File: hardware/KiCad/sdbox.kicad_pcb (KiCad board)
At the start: 2 copper layers, 55 x 59 mm, 22 parts, among them J1 DB25_Male_MountingHoles, J2 Barrel_Jack, J5 Conn_01x01, J6 Conn_01x01, Q1 BC847BW, Q2 BC847BW, U1 Arduino_Nano_V3, U2 Micro_SD_Card_Module, U3 PVG612S

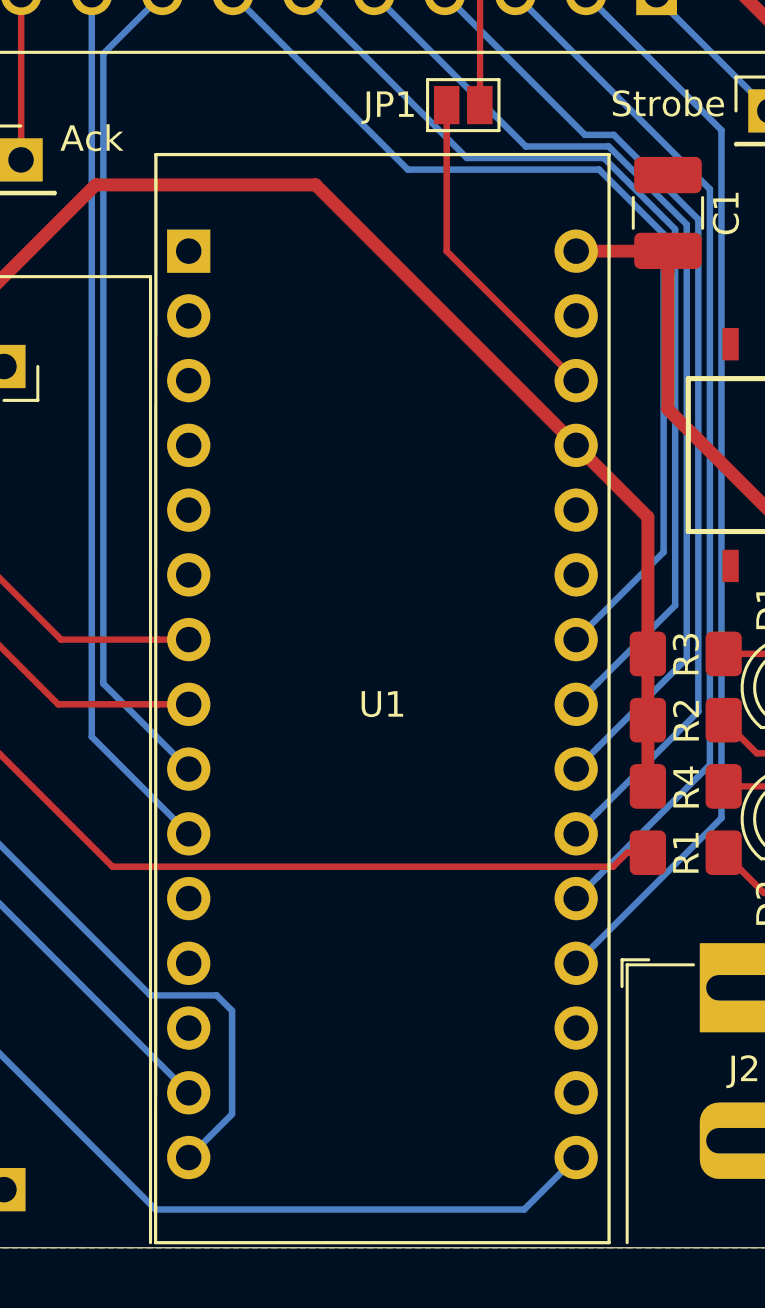
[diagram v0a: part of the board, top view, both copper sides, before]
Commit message: fixed symbol and footprint libs now included as project libs
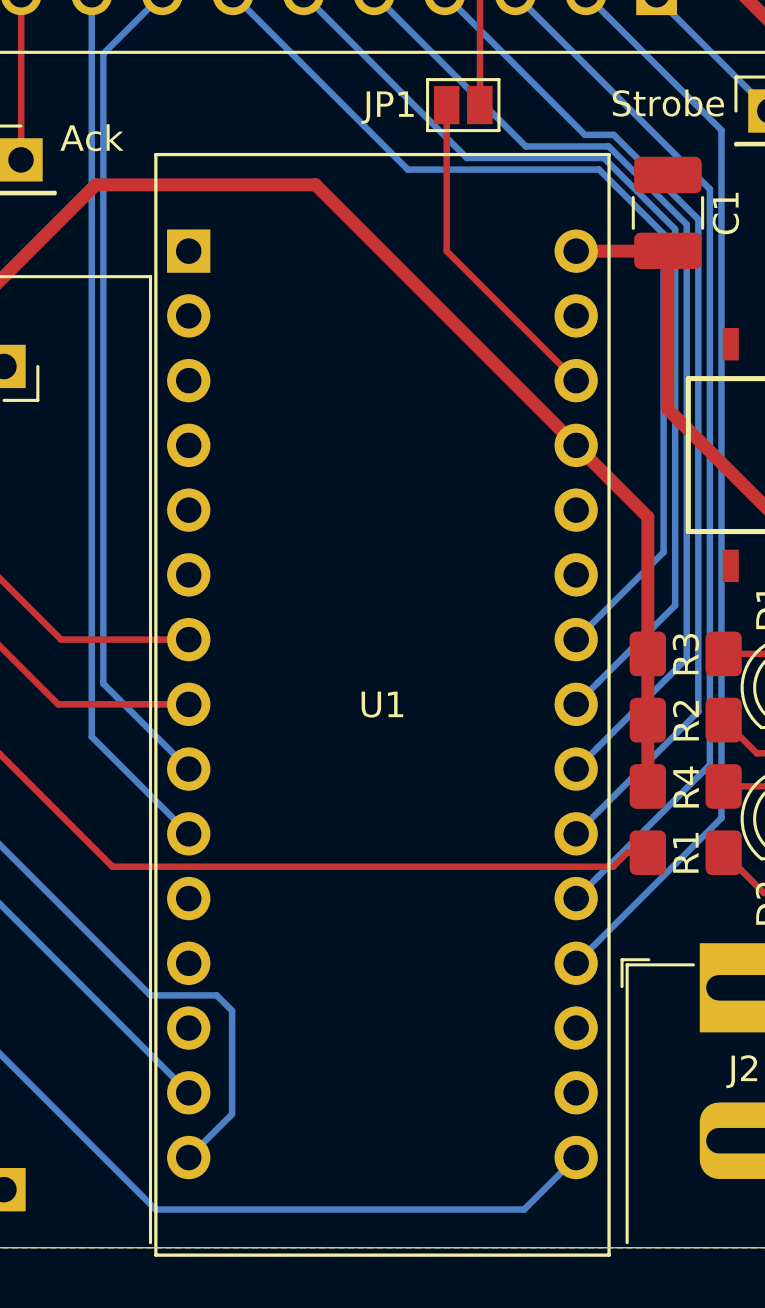
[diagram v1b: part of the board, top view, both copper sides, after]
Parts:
- R5: footprint Capacitor_SMD:C_1206_3216Metric_Pad1.42x1.75mm_HandSolder -> Resistor_SMD:R_1206_3216Metric_Pad1.42x1.75mm_HandSolder
- U1: footprint Arduino:Arduino_Nano_V3_Schield -> sdbox:Arduino_Nano_V3_Schield
- U3: footprint Relay_SMD:SOIC254P978X443-6N -> sdbox:SOIC254P978X443-6N
- renumbered Strobe to J3, Ack to J4
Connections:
- J1 pad 0: (no net) -> Net-(J1-Pad0)
- J1 pad 15: (no net) -> Net-(J1-Pad15)
- J1 pad 23: (no net) -> Net-(J1-Pad23)
- J1 pad 24: (no net) -> Net-(J1-Pad24)
- J1 pad 25: (no net) -> Net-(J1-Pad25)
- J5 pad 1: (no net) -> Net-(J5-Pad1)
- J6 pad 1: (no net) -> Net-(J6-Pad1)
- U1 pad 1: (no net) -> Net-(U1-Pad1)
- U1 pad 11: (no net) -> Net-(U1-Pad11)
- U1 pad 12: (no net) -> Net-(U1-Pad12)
- U1 pad 13: (no net) -> Net-(U1-Pad13)
- U1 pad 17: (no net) -> Net-(U1-Pad17)
- U1 pad 18: (no net) -> Net-(U1-Pad18)
- U1 pad 2: (no net) -> Net-(U1-Pad2)
- U1 pad 25: (no net) -> Net-(U1-Pad25)
- U1 pad 26: (no net) -> Net-(U1-Pad26)
- U1 pad 3: (no net) -> Net-(U1-Pad3)
- U1 pad 5: (no net) -> Net-(U1-Pad5)
- U1 pad 6: (no net) -> Net-(U1-Pad6)
- U3 pad 3: (no net) -> Net-(U3-Pad3)
- U3 pad 4: (no net) -> Net-(U3-Pad4)
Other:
- board text added: "Ack"
- board text added: "Strobe"
